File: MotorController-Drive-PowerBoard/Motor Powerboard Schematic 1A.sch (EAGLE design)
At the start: 72 parts, among them J3 APP_2POS_CONFIG5V_HORIZ, Q1 MOSFET-NCHANNELFQP30N06L, Q2 MOSFET-NCHANNELFQP30N06L, Q3 MOSFET-NCHANNELFQP30N06L, Q4 MOSFET-NCHANNELFQP30N06L, Q5 MOSFET-NCHANNELFQP30N06L, Q6 MOSFET-NCHANNELFQP30N06L, U1 NUP4201MR6

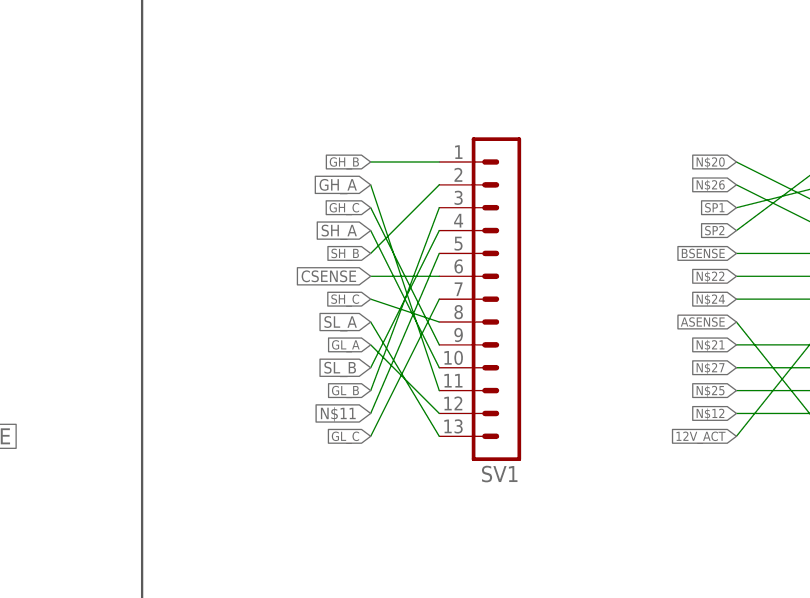
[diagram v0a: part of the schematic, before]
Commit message: Rearanged Board and rounded edges
Put Anderson Connectors in correct places as well as rewired the whole board. I then rounded the corners of the board and put wholes in the board so we could properly mount it. Eagle would not allow .144 inch holes to be drilled, but .143985 inch holes. Should be precise enough.. The headers are now spaced correctly apart and there should be enough space for the control card to sit on top of it now. Polygons were also redrawn and the board is much smaller now.  It passed the design rules check as well, so it should be almost ready. Whenever Control card is finished, pin assignments may need to be changed, other than that, the board could technically go into production.
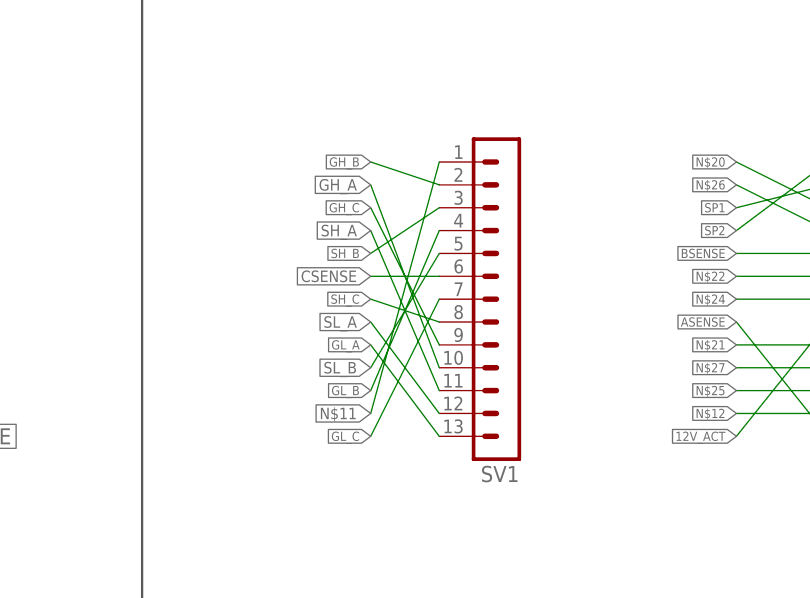
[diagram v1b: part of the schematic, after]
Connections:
- net GH_A: now also SV1.10; no longer SV1.11
- net GH_B: now also SV1.2; no longer SV1.1
- net GL_A: now also SV1.13; no longer SV1.12
- net GL_B: now also SV1.4; no longer SV1.3
- net N$11: now also SV1.1; no longer SV1.5
- net SH_A: now also SV1.11; no longer SV1.10
- net SH_B: now also SV1.3; no longer SV1.2
- net SL_A: now also SV1.12; no longer SV1.13
- net SL_B: now also SV1.5; no longer SV1.4
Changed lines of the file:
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@@
 </segment>
 <segment>
-<pinref part="SV1" gate="G$1" pin="13"/>
-<wire x1="172.72" y1="-43.18" x2="165.1" y2="-30.48" width="0.1524" layer="91"/>
+<pinref part="SV1" gate="G$1" pin="12"/>
+<wire x1="172.72" y1="-40.64" x2="165.1" y2="-30.48" width="0.1524" layer="91"/>
 <label x="165.1" y="-30.48" size="1.27" layer="95" rot="R180" xref="yes"/>
 </segment>
@@
 </segment>
 <segment>
-<pinref part="SV1" gate="G$1" pin="12"/>
-<wire x1="172.72" y1="-40.64" x2="165.1" y2="-33.02" width="0.1524" layer="91"/>
+<pinref part="SV1" gate="G$1" pin="13"/>
+<wire x1="172.72" y1="-43.18" x2="165.1" y2="-33.02" width="0.1524" layer="91"/>
 <label x="165.1" y="-33.02" size="1.016" layer="95" rot="R180" xref="yes"/>
 </segment>
@@
 </segment>
 <segment>
-<pinref part="SV1" gate="G$1" pin="11"/>
-<wire x1="172.72" y1="-38.1" x2="165.1" y2="-15.24" width="0.1524" layer="91"/>
+<pinref part="SV1" gate="G$1" pin="10"/>
+<wire x1="172.72" y1="-35.56" x2="165.1" y2="-15.24" width="0.1524" layer="91"/>
 <label x="165.1" y="-15.24" size="1.27" layer="95" rot="R180" xref="yes"/>
 </segment>
@@
 </segment>
 <segment>
-<pinref part="SV1" gate="G$1" pin="10"/>
-<wire x1="172.72" y1="-35.56" x2="165.1" y2="-20.32" width="0.1524" layer="91"/>
+<pinref part="SV1" gate="G$1" pin="11"/>
+<wire x1="172.72" y1="-38.1" x2="165.1" y2="-20.32" width="0.1524" layer="91"/>
 <label x="165.1" y="-20.32" size="1.27" layer="95" rot="R180" xref="yes"/>
 </segment>
@@
 </segment>
 <segment>
-<pinref part="SV1" gate="G$1" pin="4"/>
-<wire x1="172.72" y1="-20.32" x2="165.1" y2="-35.56" width="0.1524" layer="91"/>
+<pinref part="SV1" gate="G$1" pin="5"/>
+<wire x1="172.72" y1="-22.86" x2="165.1" y2="-35.56" width="0.1524" layer="91"/>
 <label x="165.1" y="-35.56" size="1.27" layer="95" rot="R180" xref="yes"/>
 </segment>
@@
 </segment>
 <segment>
-<pinref part="SV1" gate="G$1" pin="3"/>
-<wire x1="172.72" y1="-17.78" x2="165.1" y2="-38.1" width="0.1524" layer="91"/>
+<pinref part="SV1" gate="G$1" pin="4"/>
+<wire x1="172.72" y1="-20.32" x2="165.1" y2="-38.1" width="0.1524" layer="91"/>
 <label x="165.1" y="-38.1" size="1.016" layer="95" rot="R180" xref="yes"/>
 </segment>
@@
 </segment>
 <segment>
-<pinref part="SV1" gate="G$1" pin="1"/>
-<wire x1="172.72" y1="-12.7" x2="165.1" y2="-12.7" width="0.1524" layer="91"/>
+<pinref part="SV1" gate="G$1" pin="2"/>
+<wire x1="172.72" y1="-15.24" x2="165.1" y2="-12.7" width="0.1524" layer="91"/>
 <label x="165.1" y="-12.7" size="1.016" layer="95" rot="R180" xref="yes"/>
 </segment>
@@
 </segment>
 <segment>
-<pinref part="SV1" gate="G$1" pin="2"/>
-<wire x1="172.72" y1="-15.24" x2="165.1" y2="-22.86" width="0.1524" layer="91"/>
+<pinref part="SV1" gate="G$1" pin="3"/>
+<wire x1="172.72" y1="-17.78" x2="165.1" y2="-22.86" width="0.1524" layer="91"/>
 <label x="165.1" y="-22.86" size="1.016" layer="95" rot="R180" xref="yes"/>
 </segment>
@@
 <net name="N$11" class="0">
 <segment>
-<pinref part="SV1" gate="G$1" pin="5"/>
-<wire x1="172.72" y1="-22.86" x2="165.1" y2="-40.64" width="0.1524" layer="91"/>
+<pinref part="SV1" gate="G$1" pin="1"/>
+<wire x1="172.72" y1="-12.7" x2="165.1" y2="-40.64" width="0.1524" layer="91"/>
 <label x="165.1" y="-40.64" size="1.27" layer="95" rot="R180" xref="yes"/>
 </segment>

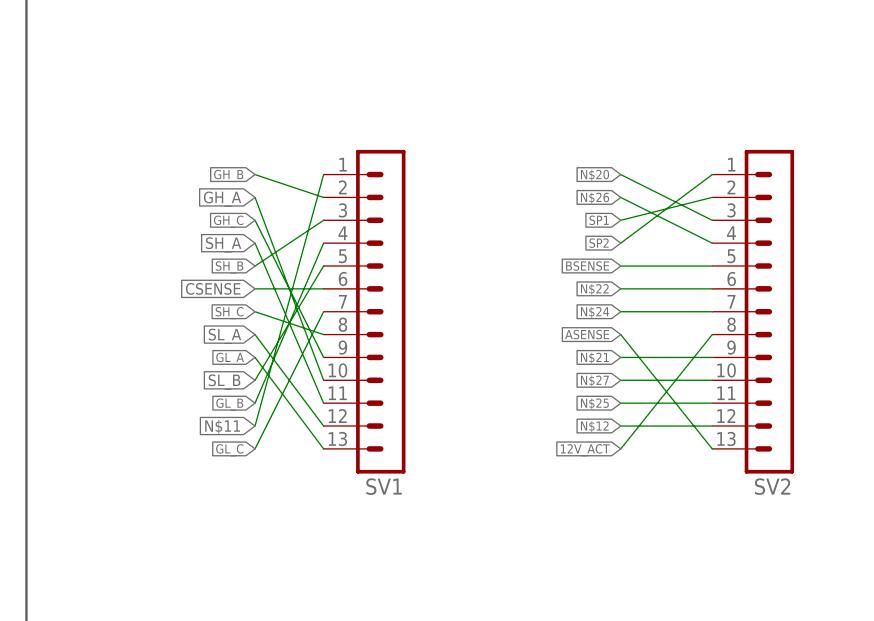
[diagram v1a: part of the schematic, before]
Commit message: Fixed holes and schematic pins
Board is now about ready for production, will need to change based on control card. Things to consider are caps, possible bigger uF and less caps. Will need to debate about that due to heighth issue.
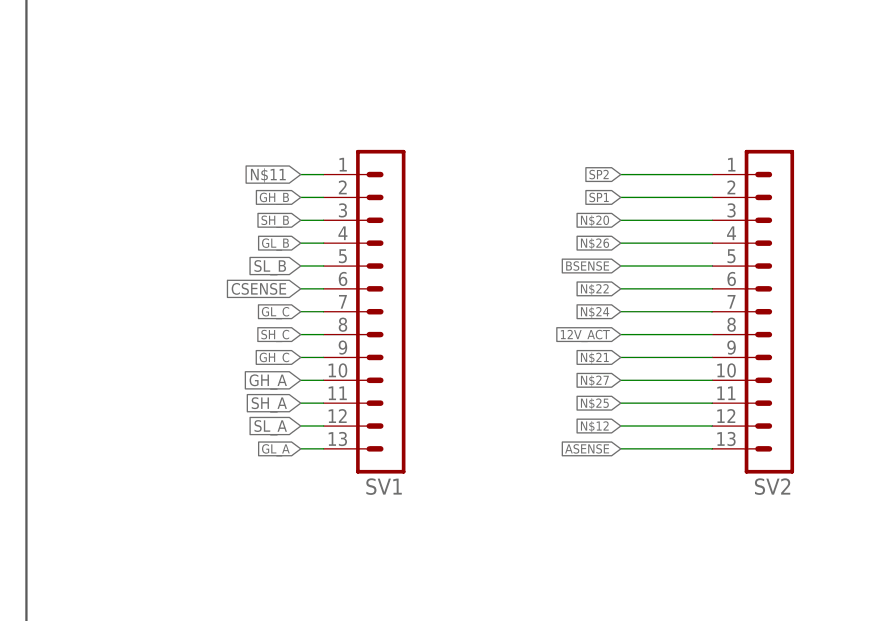
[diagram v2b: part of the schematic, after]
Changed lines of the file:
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@@
 <segment>
 <pinref part="SV2" gate="G$1" pin="8"/>
-<wire x1="215.9" y1="-30.48" x2="205.74" y2="-43.18" width="0.1524" layer="91"/>
-<label x="205.74" y="-43.18" size="1.016" layer="95" rot="R180" xref="yes"/>
+<wire x1="215.9" y1="-30.48" x2="205.74" y2="-30.48" width="0.1524" layer="91"/>
+<label x="205.74" y="-30.48" size="1.016" layer="95" rot="R180" xref="yes"/>
 </segment>
 </net>
@@
 <segment>
 <pinref part="SV2" gate="G$1" pin="13"/>
-<wire x1="215.9" y1="-43.18" x2="205.74" y2="-30.48" width="0.1524" layer="91"/>
-<label x="205.74" y="-30.48" size="1.016" layer="95" rot="R180" xref="yes"/>
+<wire x1="215.9" y1="-43.18" x2="205.74" y2="-43.18" width="0.1524" layer="91"/>
+<label x="205.74" y="-43.18" size="1.016" layer="95" rot="R180" xref="yes"/>
 </segment>
 </net>
@@
 <segment>
 <pinref part="SV1" gate="G$1" pin="6"/>
-<wire x1="172.72" y1="-25.4" x2="165.1" y2="-25.4" width="0.1524" layer="91"/>
-<label x="165.1" y="-25.4" size="1.27" layer="95" rot="R180" xref="yes"/>
+<wire x1="172.72" y1="-25.4" x2="170.18" y2="-25.4" width="0.1524" layer="91"/>
+<label x="170.18" y="-25.4" size="1.27" layer="95" rot="R180" xref="yes"/>
 </segment>
 </net>
@@
 <segment>
 <pinref part="SV1" gate="G$1" pin="12"/>
-<wire x1="172.72" y1="-40.64" x2="165.1" y2="-30.48" width="0.1524" layer="91"/>
-<label x="165.1" y="-30.48" size="1.27" layer="95" rot="R180" xref="yes"/>
+<wire x1="172.72" y1="-40.64" x2="170.18" y2="-40.64" width="0.1524" layer="91"/>
+<label x="170.18" y="-40.64" size="1.27" layer="95" rot="R180" xref="yes"/>
 </segment>
 </net>
@@
 <segment>
 <pinref part="SV1" gate="G$1" pin="13"/>
-<wire x1="172.72" y1="-43.18" x2="165.1" y2="-33.02" width="0.1524" layer="91"/>
-<label x="165.1" y="-33.02" size="1.016" layer="95" rot="R180" xref="yes"/>
+<wire x1="172.72" y1="-43.18" x2="170.18" y2="-43.18" width="0.1524" layer="91"/>
+<label x="170.18" y="-43.18" size="1.016" layer="95" rot="R180" xref="yes"/>
 </segment>
 </net>
@@
 <segment>
 <pinref part="SV1" gate="G$1" pin="10"/>
-<wire x1="172.72" y1="-35.56" x2="165.1" y2="-15.24" width="0.1524" layer="91"/>
-<label x="165.1" y="-15.24" size="1.27" layer="95" rot="R180" xref="yes"/>
+<wire x1="172.72" y1="-35.56" x2="170.18" y2="-35.56" width="0.1524" layer="91"/>
+<label x="170.18" y="-35.56" size="1.27" layer="95" rot="R180" xref="yes"/>
 </segment>
 </net>
@@
 <segment>
 <pinref part="SV1" gate="G$1" pin="11"/>
-<wire x1="172.72" y1="-38.1" x2="165.1" y2="-20.32" width="0.1524" layer="91"/>
-<label x="165.1" y="-20.32" size="1.27" layer="95" rot="R180" xref="yes"/>
+<wire x1="172.72" y1="-38.1" x2="170.18" y2="-38.1" width="0.1524" layer="91"/>
+<label x="170.18" y="-38.1" size="1.27" layer="95" rot="R180" xref="yes"/>
 </segment>
 </net>
@@
 <segment>
 <pinref part="SV1" gate="G$1" pin="5"/>
-<wire x1="172.72" y1="-22.86" x2="165.1" y2="-35.56" width="0.1524" layer="91"/>
-<label x="165.1" y="-35.56" size="1.27" layer="95" rot="R180" xref="yes"/>
+<wire x1="172.72" y1="-22.86" x2="170.18" y2="-22.86" width="0.1524" layer="91"/>
+<label x="170.18" y="-22.86" size="1.27" layer="95" rot="R180" xref="yes"/>
 </segment>
 </net>
@@
 <segment>
 <pinref part="SV1" gate="G$1" pin="4"/>
-<wire x1="172.72" y1="-20.32" x2="165.1" y2="-38.1" width="0.1524" layer="91"/>
-<label x="165.1" y="-38.1" size="1.016" layer="95" rot="R180" xref="yes"/>
+<wire x1="172.72" y1="-20.32" x2="170.18" y2="-20.32" width="0.1524" layer="91"/>
+<label x="170.18" y="-20.32" size="1.016" layer="95" rot="R180" xref="yes"/>
 </segment>
 </net>
@@
 <segment>
 <pinref part="SV1" gate="G$1" pin="2"/>
-<wire x1="172.72" y1="-15.24" x2="165.1" y2="-12.7" width="0.1524" layer="91"/>
-<label x="165.1" y="-12.7" size="1.016" layer="95" rot="R180" xref="yes"/>
+<wire x1="172.72" y1="-15.24" x2="170.18" y2="-15.24" width="0.1524" layer="91"/>
+<label x="170.18" y="-15.24" size="1.016" layer="95" rot="R180" xref="yes"/>
 </segment>
 </net>
@@
 <segment>
 <pinref part="SV1" gate="G$1" pin="3"/>
-<wire x1="172.72" y1="-17.78" x2="165.1" y2="-22.86" width="0.1524" layer="91"/>
-<label x="165.1" y="-22.86" size="1.016" layer="95" rot="R180" xref="yes"/>
+<wire x1="172.72" y1="-17.78" x2="170.18" y2="-17.78" width="0.1524" layer="91"/>
+<label x="170.18" y="-17.78" size="1.016" layer="95" rot="R180" xref="yes"/>
 </segment>
 </net>
@@
 <segment>
 <pinref part="SV1" gate="G$1" pin="7"/>
-<wire x1="172.72" y1="-27.94" x2="165.1" y2="-43.18" width="0.1524" layer="91"/>
-<label x="165.1" y="-43.18" size="1.016" layer="95" rot="R180" xref="yes"/>
+<wire x1="172.72" y1="-27.94" x2="170.18" y2="-27.94" width="0.1524" layer="91"/>
+<label x="170.18" y="-27.94" size="1.016" layer="95" rot="R180" xref="yes"/>
 </segment>
 </net>
@@
 <segment>
 <pinref part="SV1" gate="G$1" pin="8"/>
-<wire x1="172.72" y1="-30.48" x2="165.1" y2="-27.94" width="0.1524" layer="91"/>
-<label x="165.1" y="-27.94" size="1.016" layer="95" rot="R180" xref="yes"/>
+<wire x1="172.72" y1="-30.48" x2="170.18" y2="-30.48" width="0.1524" layer="91"/>
+<label x="170.18" y="-30.48" size="1.016" layer="95" rot="R180" xref="yes"/>
 </segment>
 </net>
@@
 <segment>
 <pinref part="SV1" gate="G$1" pin="9"/>
-<wire x1="172.72" y1="-33.02" x2="165.1" y2="-17.78" width="0.1524" layer="91"/>
-<label x="165.1" y="-17.78" size="1.016" layer="95" rot="R180" xref="yes"/>
+<wire x1="172.72" y1="-33.02" x2="170.18" y2="-33.02" width="0.1524" layer="91"/>
+<label x="170.18" y="-33.02" size="1.016" layer="95" rot="R180" xref="yes"/>
 </segment>
 </net>
@@
 <segment>
 <pinref part="SV2" gate="G$1" pin="2"/>
-<wire x1="215.9" y1="-15.24" x2="205.74" y2="-17.78" width="0.1524" layer="91"/>
-<label x="205.74" y="-17.78" size="1.016" layer="95" rot="R180" xref="yes"/>
+<wire x1="215.9" y1="-15.24" x2="205.74" y2="-15.24" width="0.1524" layer="91"/>
+<label x="205.74" y="-15.24" size="1.016" layer="95" rot="R180" xref="yes"/>
 </segment>
 </net>
@@
 <segment>
 <pinref part="SV2" gate="G$1" pin="1"/>
-<wire x1="215.9" y1="-12.7" x2="205.74" y2="-20.32" width="0.1524" layer="91"/>
-<label x="205.74" y="-20.32" size="1.016" layer="95" rot="R180" xref="yes"/>
+<wire x1="215.9" y1="-12.7" x2="205.74" y2="-12.7" width="0.1524" layer="91"/>
+<label x="205.74" y="-12.7" size="1.016" layer="95" rot="R180" xref="yes"/>
 </segment>
 </net>
@@
 <segment>
 <pinref part="SV1" gate="G$1" pin="1"/>
-<wire x1="172.72" y1="-12.7" x2="165.1" y2="-40.64" width="0.1524" layer="91"/>
-<label x="165.1" y="-40.64" size="1.27" layer="95" rot="R180" xref="yes"/>
+<wire x1="172.72" y1="-12.7" x2="170.18" y2="-12.7" width="0.1524" layer="91"/>
+<label x="170.18" y="-12.7" size="1.27" layer="95" rot="R180" xref="yes"/>
 </segment>
 </net>
@@
 <segment>
 <pinref part="SV2" gate="G$1" pin="4"/>
-<wire x1="215.9" y1="-20.32" x2="205.74" y2="-15.24" width="0.1524" layer="91"/>
-<label x="205.74" y="-15.24" size="1.016" layer="95" rot="R180" xref="yes"/>
+<wire x1="215.9" y1="-20.32" x2="205.74" y2="-20.32" width="0.1524" layer="91"/>
+<label x="205.74" y="-20.32" size="1.016" layer="95" rot="R180" xref="yes"/>
 </segment>
 </net>
@@
 <segment>
 <pinref part="SV2" gate="G$1" pin="3"/>
-<wire x1="215.9" y1="-17.78" x2="205.74" y2="-12.7" width="0.1524" layer="91"/>
-<label x="205.74" y="-12.7" size="1.016" layer="95" rot="R180" xref="yes"/>
-</segment>
-</net>
+<wire x1="215.9" y1="-17.78" x2="205.74" y2="-17.78" width="0.1524" layer="91"/>
+<label x="205.74" y="-17.78" size="1.016" layer="95" rot="R180" xref="yes"/>
+</segment>
+</net>

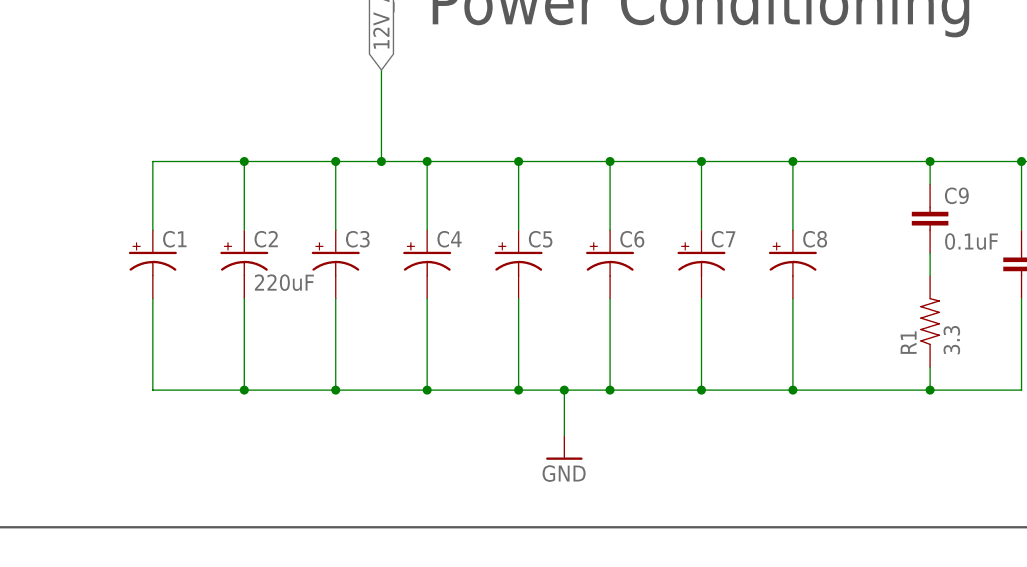
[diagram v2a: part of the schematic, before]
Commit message: Fets are now foldable
Had to move caps around to get fets ample space to be able to be folded down under the board. Approximately 20mm of space. Will still need changes as top chip is finished. Power now has to round several tight corners instead of a straight flow.
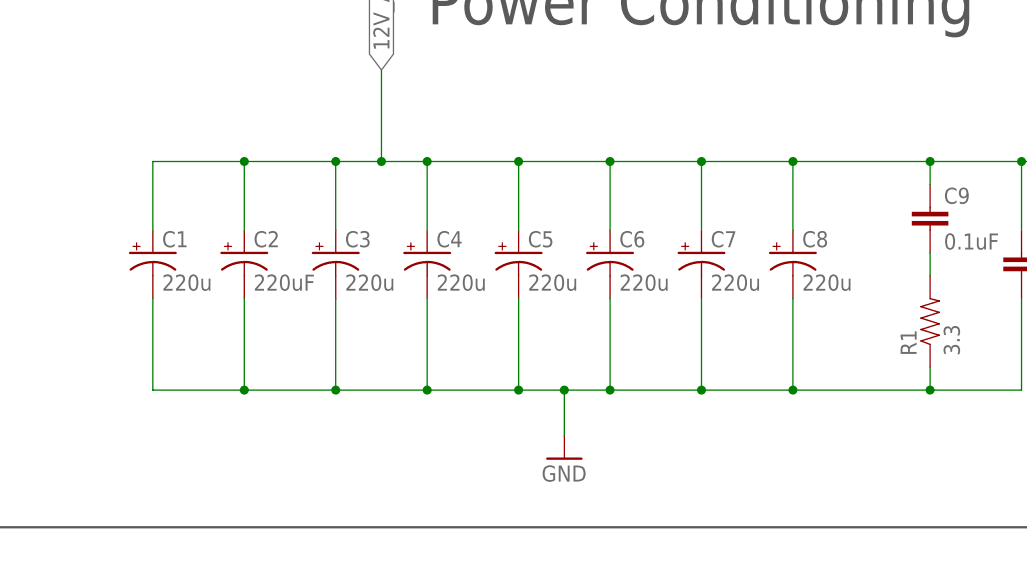
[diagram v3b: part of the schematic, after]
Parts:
- C1, C3, C4, C5, C6, C7, C8: value (none) -> 220u
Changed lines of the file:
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@@
 </classes>
 <parts>
-<part name="C1" library="SparkFun-Passives" deviceset="CAP_POL" device="PTH4"/>
+<part name="C1" library="SparkFun-Passives" deviceset="CAP_POL" device="PTH4" value="220u"/>
 <part name="C2" library="SparkFun-Passives" deviceset="CAP_POL" device="PTH4" value="220uF"/>
-<part name="C3" library="SparkFun-Passives" deviceset="CAP_POL" device="PTH4"/>
-<part name="C4" library="SparkFun-Passives" deviceset="CAP_POL" device="PTH4"/>
-<part name="C5" library="SparkFun-Passives" deviceset="CAP_POL" device="PTH4"/>
-<part name="C6" library="SparkFun-Passives" deviceset="CAP_POL" device="PTH4"/>
-<part name="C7" library="SparkFun-Passives" deviceset="CAP_POL" device="PTH4"/>
-<part name="C8" library="SparkFun-Passives" deviceset="CAP_POL" device="PTH4"/>
+<part name="C3" library="SparkFun-Passives" deviceset="CAP_POL" device="PTH4" value="220u"/>
+<part name="C4" library="SparkFun-Passives" deviceset="CAP_POL" device="PTH4" value="220u"/>
+<part name="C5" library="SparkFun-Passives" deviceset="CAP_POL" device="PTH4" value="220u"/>
+<part name="C6" library="SparkFun-Passives" deviceset="CAP_POL" device="PTH4" value="220u"/>
+<part name="C7" library="SparkFun-Passives" deviceset="CAP_POL" device="PTH4" value="220u"/>
+<part name="C8" library="SparkFun-Passives" deviceset="CAP_POL" device="PTH4" value="220u"/>
 <part name="R1" library="SparkFun-Passives" deviceset="RESISTOR" device="1206" value="3.3"/>
 <part name="GND1" library="SparkFun-Aesthetics" deviceset="GND" device=""/>

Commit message: Added 2 layers for routing convenience
Board Review suggested adding layers to promote larger traces for power. Power now is correctly labelled. Things to still add. Silkscreen labeling, as well as checking package on Anderson Connectors.
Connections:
- net 12V_ACT renamed PCK_VOLT
- net 12V_ACT_SENSE renamed PCK_VOLT_SENSE
- net GH_A: now also SV1.12; no longer SV1.10
- net GL_A: now also SV1.11; no longer SV1.13
- net SH_A: now also SV1.10; no longer SV1.11
- net SL_A: now also SV1.13; no longer SV1.12
